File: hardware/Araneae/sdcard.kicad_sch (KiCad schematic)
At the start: 4 parts, among them J12 Micro_SD_Card, U21 RT9742GGJ5

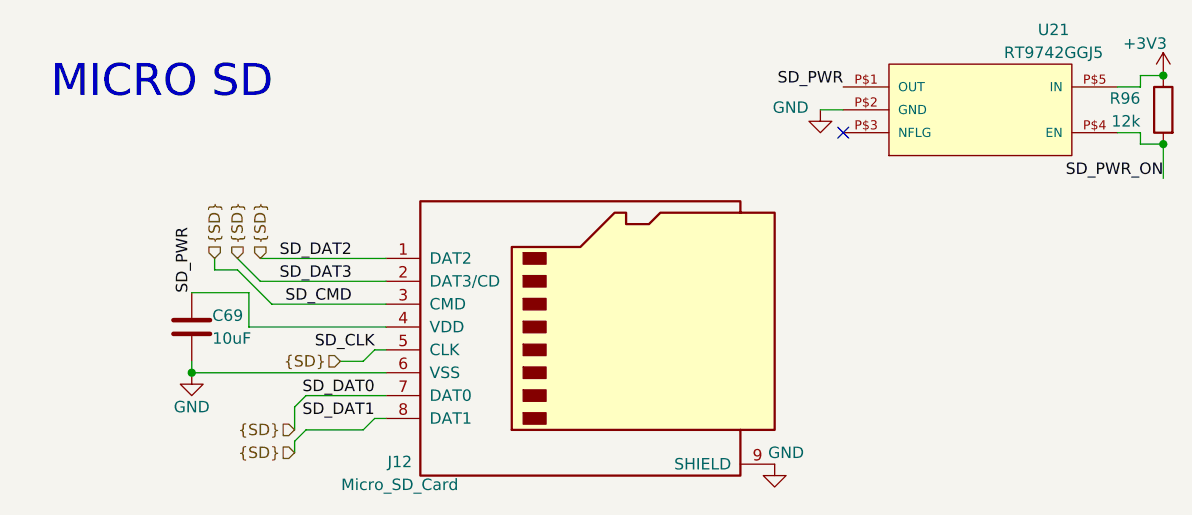
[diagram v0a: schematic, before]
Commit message: Add CI workflow for PCB checks and artifact generation
- Created a GitHub Actions workflow (`ci.yml`) to automate hardware checks including ERC, DRC, and plot generation for KiCad projects.
- Added a new footprint for the SON50P200X200X80-9N component in `SON50P200X200X80-9N.kicad_mod`.
- Introduced a new symbol for the TPS22965DSGR component in `TPS22965DSGR.kicad_sym`.
- Added a configuration file `kibot.yaml` for generating fabrication files and other outputs.
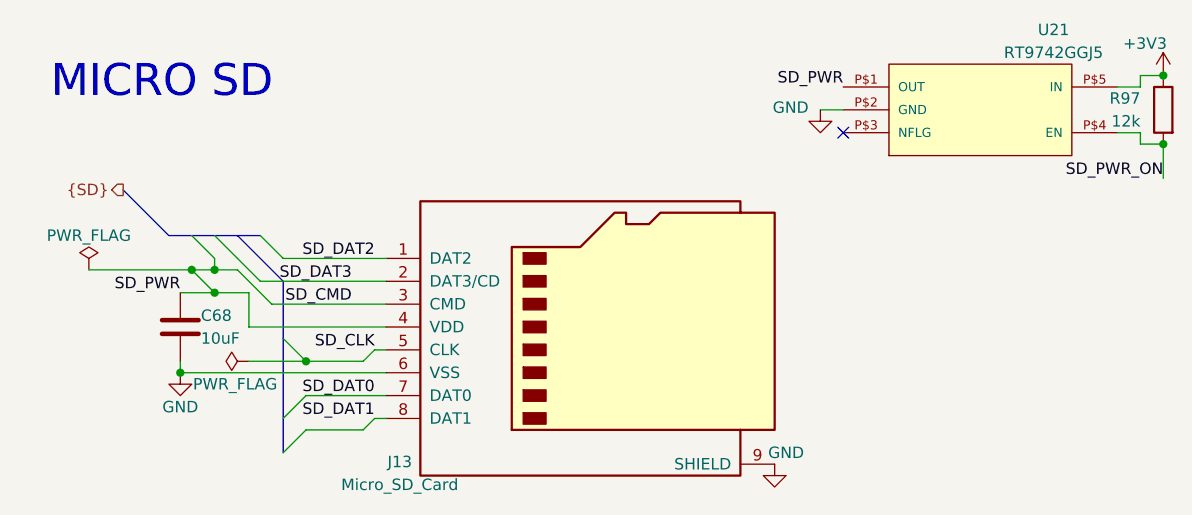
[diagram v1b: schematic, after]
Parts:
- C68: renamed from C69; footprint (none) -> Capacitor_SMD:C_0603_1608Metric
- J13: renamed from J12; footprint (none) -> Connector_Card:microSD_HC_Hirose_DM3D-SF
- R97: renamed from R96; footprint (none) -> Resistor_SMD:R_0603_1608Metric
- U21: footprint RT9742GGJ5:TSOT-23-5 -> OPL:TSOT-23-5
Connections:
- net {SD}: no longer J13.1 (DAT2), J13.2 (DAT3/CD), J13.3 (CMD), J13.5 (CLK), J13.7 (DAT0), J13.8 (DAT1)
- net SD_PWR renamed SD_CMD
- net SD_CMD: now also J13.3 (CMD)
- new net SD_CLK: J13.5 (CLK)
- new net SD_DAT0: J13.7 (DAT0)
- new net SD_DAT1: J13.8 (DAT1)
- new net SD_DAT2: J13.1 (DAT2)
- new net SD_DAT3: J13.2 (DAT3/CD)
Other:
- company: (none) -> Matheus Henrique(Aka: TheusHen)
- title: (none) -> Araneae
- moved on the sheet: C68
